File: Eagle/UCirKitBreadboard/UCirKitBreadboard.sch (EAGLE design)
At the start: 80 parts

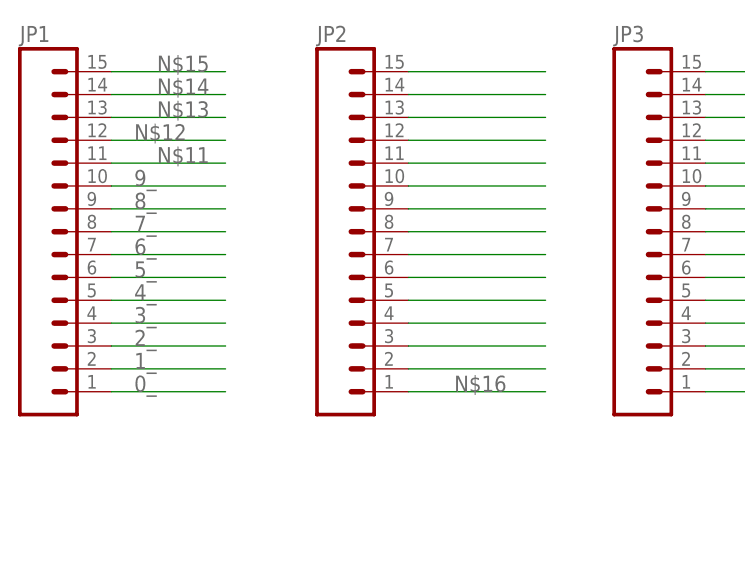
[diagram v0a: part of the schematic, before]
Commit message: RenameAllNetToClean.ulp script uploaded
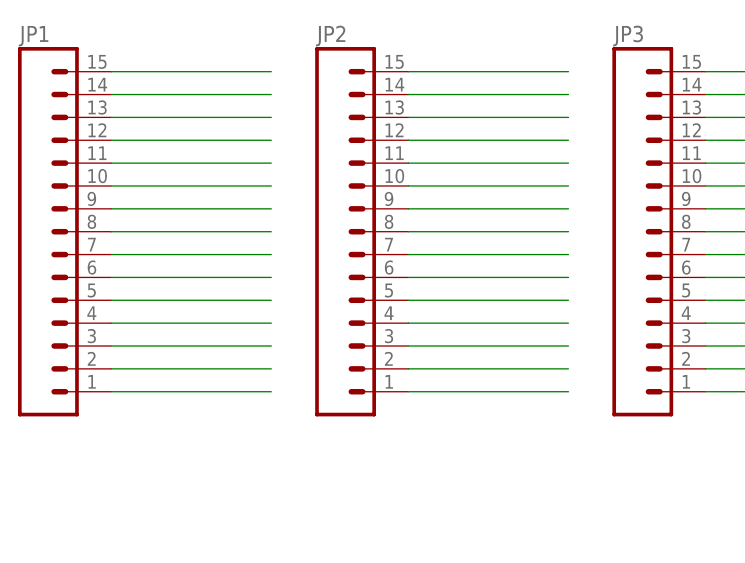
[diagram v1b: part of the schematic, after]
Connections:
- new net N$1: JP1.1
- new net N$10: JP1.10
- new net N$2: JP1.2
- new net N$3: JP1.3
- new net N$4: JP1.4
- new net N$5: JP1.5
- new net N$6: JP1.6
- new net N$7: JP1.7
- new net N$8: JP1.8
- new net N$9: JP1.9
- net 0_: no longer JP1.1
- net 1_: no longer JP1.2
- net 2_: no longer JP1.3
- net 3_: no longer JP1.4
- net 4_: no longer JP1.5
- net 5_: no longer JP1.6
- net 6_: no longer JP1.7
- net 7_: no longer JP1.8
- net 8_: no longer JP1.9
- net 9_: no longer JP1.10
